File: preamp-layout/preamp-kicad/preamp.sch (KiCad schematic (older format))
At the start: 13 parts, among them J1 AudioJack3, P1 Conn_WallPlug, SW1 SW_SPST, SW10 Rotary_Encoder_Switch, SW11 Rotary_Encoder_Switch, SW2 SW_Push_Open, SW3 SW_Push_Open, SW4 SW_Push_Open, SW5 SW_Push_Open, SW6 SW_Push_Open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

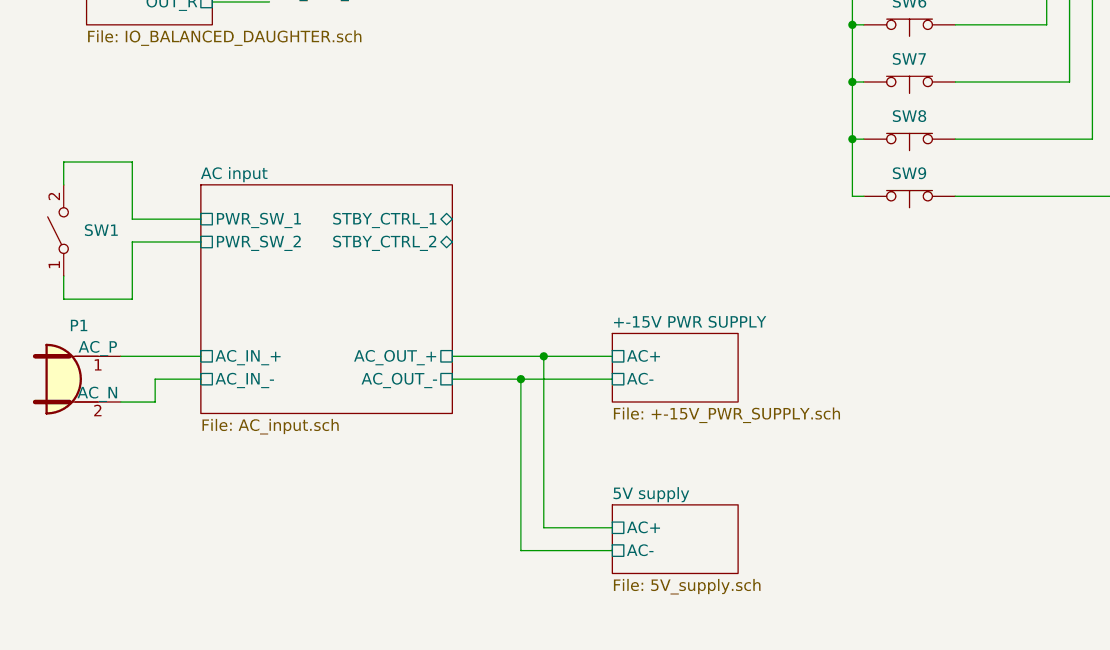
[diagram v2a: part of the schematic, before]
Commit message: Power Supply Update
Grounding made more clear, tied to chassis on AC board. Pins renamed. Aligned with AC wall power convention. General cleanup.
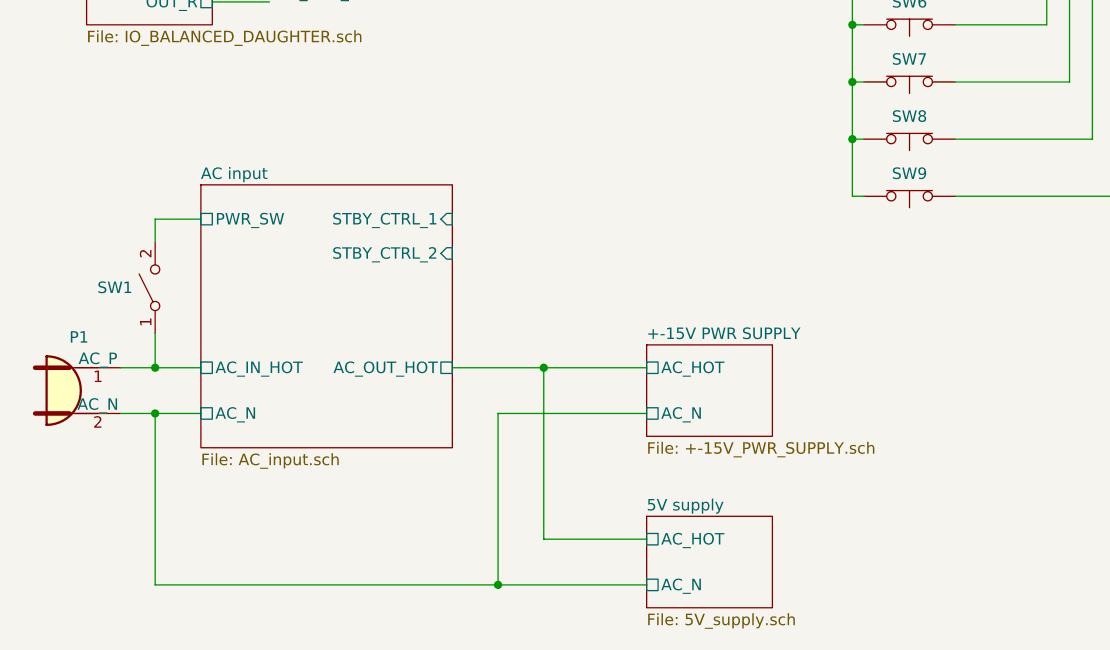
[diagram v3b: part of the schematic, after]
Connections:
- net AC input/PWR_SW_2 is gone; now on net AC input/AC_IN_HOT: SW1.1 (A)
- net AC input/AC_IN_+ renamed AC input/AC_IN_HOT
- net AC input/AC_IN_- renamed +-15V PWR SUPPLY/AC_N
- net AC input/PWR_SW_1 renamed AC input/PWR_SW
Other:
- moved on the sheet: P1, SW1
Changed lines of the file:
@@
 $EndDescr
 $Sheet
-S 1650 5650 1100 1000
+S 1650 5650 1100 1150
 U 5E26F6FE
 F0 "AC input" 50
 F1 "AC_input.sch" 50
-F2 "PWR_SW_1" U L 1650 5800 50
-F3 "PWR_SW_2" U L 1650 5900 50
-F4 "AC_OUT_+" U R 2750 6400 50
-F5 "AC_IN_-" U L 1650 6500 50
-F6 "AC_IN_+" U L 1650 6400 50
-F7 "AC_OUT_-" U R 2750 6500 50
-F8 "STBY_CTRL_2" B R 2750 5900 50
-F9 "STBY_CTRL_1" B R 2750 5800 50
-$EndSheet
-$Sheet
-S 3450 6300 550  300
+F2 "AC_OUT_HOT" U R 2750 6450 50
+F3 "AC_IN_HOT" U L 1650 6450 50
+F4 "AC_N" U L 1650 6650 50
+F5 "PWR_SW" U L 1650 5800 50
+F6 "STBY_CTRL_2" I R 2750 5950 50
+F7 "STBY_CTRL_1" I R 2750 5800 50
+$EndSheet
+$Sheet
+S 3600 6350 550  400
 U 5E27B612
 F0 "+-15V PWR SUPPLY" 50
 F1 "+-15V_PWR_SUPPLY.sch" 50
-F2 "AC+" U L 3450 6400 50
-F3 "AC-" U L 3450 6500 50
-$EndSheet
-$Sheet
-S 3450 7050 550  300
+F2 "AC_HOT" U L 3600 6450 50
+F3 "AC_N" U L 3600 6650 50
+$EndSheet
+$Sheet
+S 3600 7100 550  400
 U 5E5EF2D4
 F0 "5V supply" 50
 F1 "5V_supply.sch" 50
-F2 "AC+" U L 3450 7150 50
-F3 "AC-" U L 3450 7250 50
+F2 "AC_HOT" U L 3600 7200 50
+F3 "AC_N" U L 3600 7400 50
 $EndSheet
 $Sheet
@@
 	8000 3500 8100 3600
 Wire Wire Line
-	2750 6400 3150 6400
-Wire Wire Line
-	2750 6500 3050 6500
-Wire Wire Line
-	3150 6400 3150 7150
-Wire Wire Line
-	3150 6400 3450 6400
-Wire Wire Line
-	3050 6500 3050 7250
-Wire Wire Line
-	3050 6500 3450 6500
+	2750 6450 3150 6450
+Wire Wire Line
+	3150 6450 3150 7200
 Wire Wire Line
 	1600 2850 2150 2850
@@
 Wire Wire Line
 	10750 2400 10750 2900
-$Comp
-L Switch:SW_SPST SW?
-U 1 1 5E2E8D21
-P 1050 5850
-AR Path="/5E26F6FE/5E2E8D21" Ref="SW?"  Part="1"
-AR Path="/5E2E8D21" Ref="SW1"  Part="1"
-F 0 "SW1" V 1050 5762 50  0000 R CNN
-F 1 "SW_SPST" H 1050 5994 50  0001 C CNN
-F 2 "" H 1050 5850 50  0001 C CNN
-F 3 "~" H 1050 5850 50  0001 C CNN
-	1    1050 5850
-	0    -1   -1   0
-$EndComp
-Wire Wire Line
-	1050 5650 1050 5550
-Wire Wire Line
-	1050 5550 1350 5550
-Wire Wire Line
-	1350 5550 1350 5800
-Wire Wire Line
-	1350 5800 1650 5800
-Wire Wire Line
-	1050 6050 1050 6150
-Wire Wire Line
-	1050 6150 1350 6150
-Wire Wire Line
-	1350 6150 1350 5900
-Wire Wire Line
-	1350 5900 1650 5900
-$Comp
-L Connector:Conn_WallPlug P?
-U 1 1 5E300B43
-P 1100 6500
-AR Path="/5E26F6FE/5E300B43" Ref="P?"  Part="1"
-AR Path="/5E300B43" Ref="P1"  Part="1"
-F 0 "P1" H 1117 6733 50  0000 C CNN
-F 1 "Conn_WallPlug" H 1117 6734 50  0001 C CNN
-F 2 "" H 1500 6500 50  0001 C CNN
-F 3 "~" H 1500 6500 50  0001 C CNN
-	1    1100 6500
-	1    0    0    -1
-$EndComp
-Wire Wire Line
-	1300 6400 1650 6400
-Wire Wire Line
-	1300 6600 1450 6600
-Wire Wire Line
-	1450 6600 1450 6500
-Wire Wire Line
-	1450 6500 1650 6500
 $Sheet
 S 8250 4500 550  300
@@
 F5 "IN_R" U R 1700 4600 50
 $EndSheet
-Connection ~ 3050 6500
-Connection ~ 3150 6400
-Wire Wire Line
-	3450 7150 3150 7150
-Wire Wire Line
-	3450 7250 3050 7250
+Connection ~ 3150 6450
 Wire Wire Line
 	7800 3050 7800 4650
@@
 Wire Wire Line
 	7650 2900 8200 2900
+Wire Wire Line
+	1300 6650 1450 6650
+$Comp
+L Connector:Conn_WallPlug P?
+U 1 1 5E300B43
+P 1100 6550
+AR Path="/5E26F6FE/5E300B43" Ref="P?"  Part="1"
+AR Path="/5E300B43" Ref="P1"  Part="1"
+F 0 "P1" H 1117 6783 50  0000 C CNN
+F 1 "Conn_WallPlug" H 1117 6784 50  0001 C CNN
+F 2 "" H 1500 6550 50  0001 C CNN
+F 3 "~" H 1500 6550 50  0001 C CNN
+	1    1100 6550
+	1    0    0    -1
+$EndComp
+$Comp
+L Switch:SW_SPST SW?
+U 1 1 5E2E8D21
+P 1450 6100
+AR Path="/5E26F6FE/5E2E8D21" Ref="SW?"  Part="1"
+AR Path="/5E2E8D21" Ref="SW1"  Part="1"
+F 0 "SW1" V 1450 6198 50  0000 L CNN
+F 1 "SW_SPST" H 1450 6244 50  0001 C CNN
+F 2 "" H 1450 6100 50  0001 C CNN
+F 3 "~" H 1450 6100 50  0001 C CNN
+	1    1450 6100
+	0    -1   -1   0
+$EndComp
+Wire Wire Line
+	1300 6450 1450 6450
+Wire Wire Line
+	1450 5900 1450 5800
+Wire Wire Line
+	1450 5800 1650 5800
+Wire Wire Line
+	1450 6300 1450 6450
+Connection ~ 1450 6450
+Wire Wire Line
+	1450 6450 1650 6450
+Wire Wire Line
+	1450 7400 2950 7400
+Connection ~ 1450 6650
+Wire Wire Line
+	1450 6650 1650 6650
+Connection ~ 2950 7400
+Wire Wire Line
+	2950 6650 2950 7400
+Wire Wire Line
+	1450 6650 1450 7400
+Wire Wire Line
+	3150 6450 3600 6450
+Wire Wire Line
+	2950 6650 3600 6650
+Wire Wire Line
+	3150 7200 3600 7200
+Wire Wire Line
+	2950 7400 3600 7400
 Wire Bus Line
 	5200 1700 5200 3300

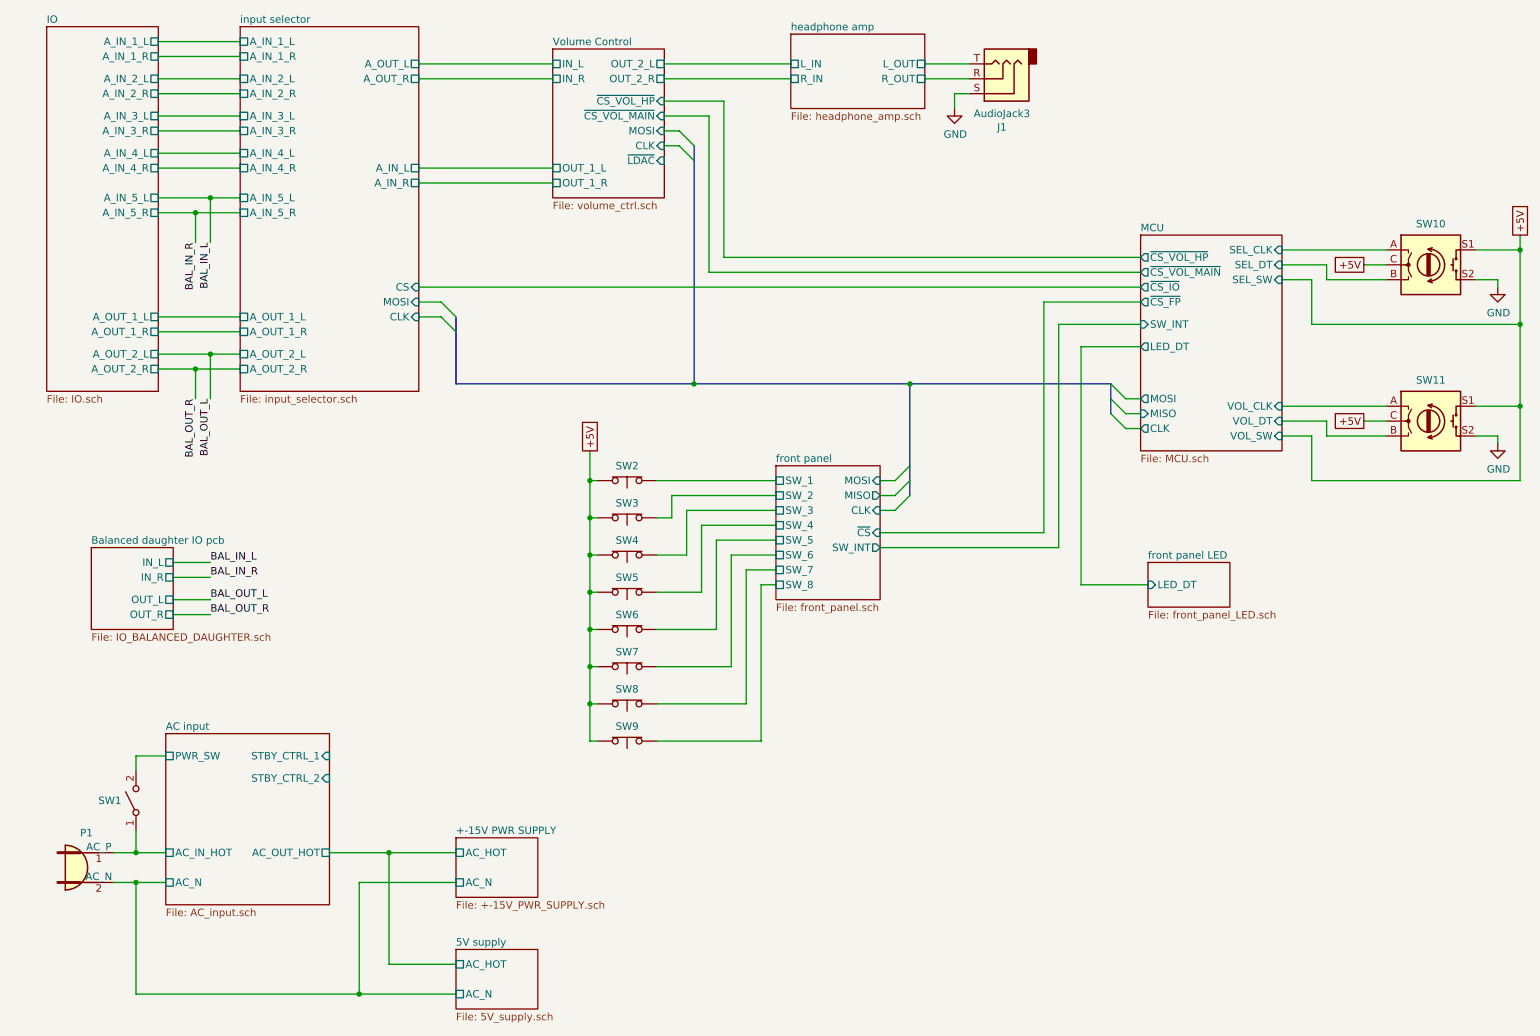
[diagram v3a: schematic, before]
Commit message: Schematic layout updates
schematic optimization. Also implemented encoders with surrounding circuitry (self-contained on encoder board)
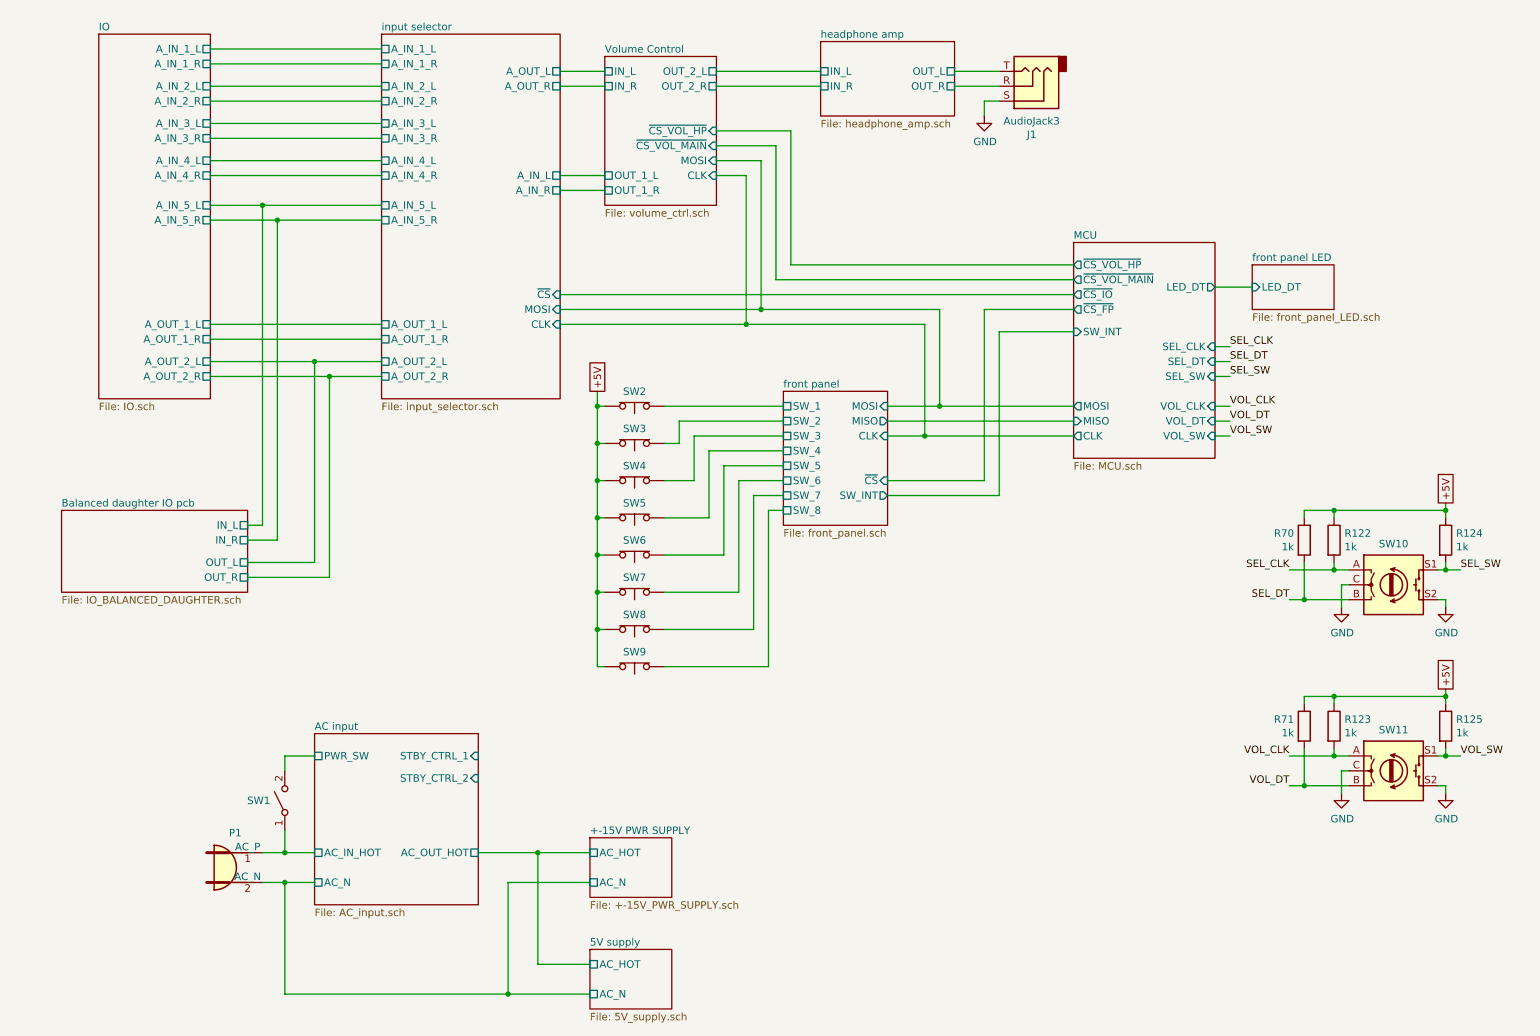
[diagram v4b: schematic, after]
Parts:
- added R122, R123, R124, R125, R70, R71: 1k, Resistor_SMD:R_1206_3216Metric_Pad1.42x1.75mm_HandSolder, symbol Device:R
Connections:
- net +5V: now also R122.1, R123.1, R124.1, R125.1, R70.1, R71.1; no longer SW10.C, SW10.S1, SW11.C, SW11.S1
- net GND: now also SW10.C, SW11.C
- net MCU/SEL_CLK renamed SEL_CLK
- net SEL_CLK: now also R122.2
- net MCU/SEL_DT renamed SEL_DT
- net SEL_DT: now also R70.2
- net MCU/VOL_CLK renamed VOL_CLK
- net VOL_CLK: now also R123.2
- net MCU/VOL_DT renamed VOL_DT
- net VOL_DT: now also R71.2
- net headphone amp/L_OUT renamed headphone amp/OUT_L
- net headphone amp/R_OUT renamed headphone amp/OUT_R
- new net SEL_SW: R124.2, SW10.S1
- new net VOL_SW: R125.2, SW11.S1
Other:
- moved on the sheet: J1, P1, SW1, SW2, SW3, SW4, SW5, SW6, SW7, SW8, SW9

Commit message: I2C init commit
Changed design from using SPI interface to I2C interface, with exception of front LED array (SPI).
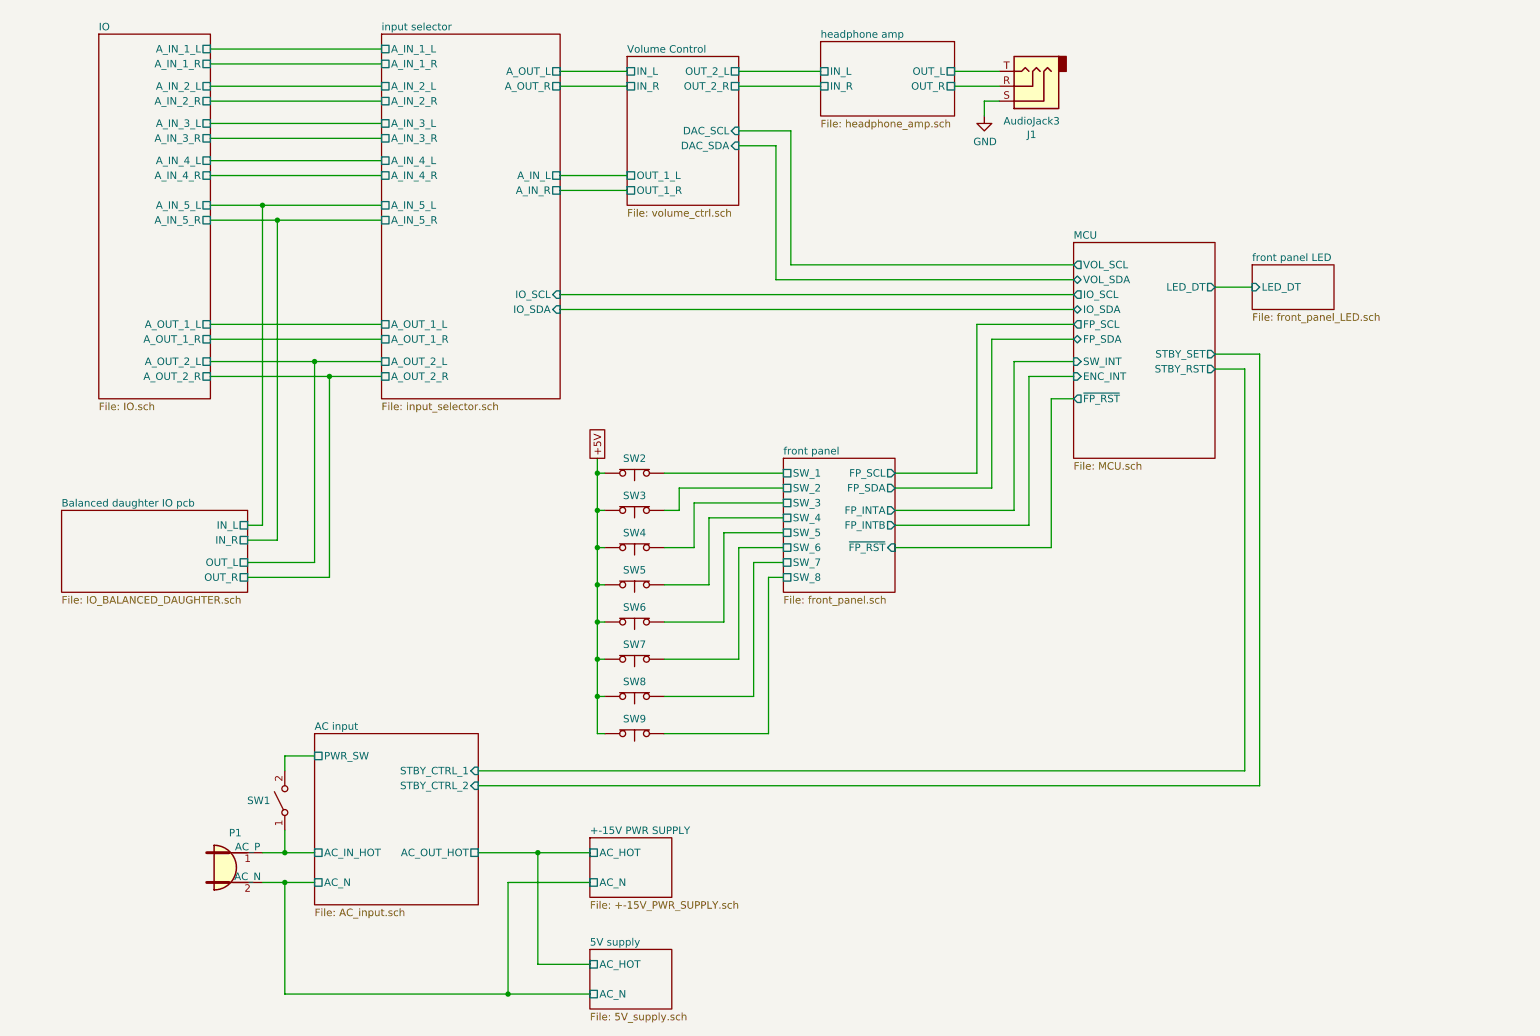
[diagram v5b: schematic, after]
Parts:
- removed R122, R123, R124, R125, R70, R71: 1k, Resistor_SMD:R_1206_3216Metric_Pad1.42x1.75mm_HandSolder, symbol Device:R
- removed SW10, SW11: Rotary_Encoder_Switch, symbol Device:Rotary_Encoder_Switch
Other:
- moved on the sheet: SW2, SW3, SW4, SW5, SW6, SW7, SW8, SW9

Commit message: BOM Update
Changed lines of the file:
@@
 $EndSheet
 $Sheet
-S 7750 2350 950  1450
+S 7750 2350 950  1200
 U 619FA14B
 F0 "MCU" 50

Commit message: Minor Updates
Moved headphone jack to amp pcb. I2C pin updates. Added caps to LED light strip. Added 0.1uF caps to all ICs.
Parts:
- removed J1: AudioJack3, symbol Connector:AudioJack3
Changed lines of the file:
@@
-$EndSheet
-$Sheet
-S 5800 3800 750  900
-U 5E5ECAAE
-F0 "front panel" 50
-F1 "front_panel.sch" 50
-F2 "SW_1" U L 5800 3900 50
-F3 "SW_2" U L 5800 4000 50
-F4 "SW_3" U L 5800 4100 50
-F5 "SW_4" U L 5800 4200 50
-F6 "SW_5" U L 5800 4300 50
-F7 "SW_6" U L 5800 4400 50
-F8 "SW_7" U L 5800 4500 50
-F9 "SW_8" U L 5800 4600 50
-F10 "FP_INTB" O R 6550 4250 50
-F11 "FP_SCL" O R 6550 3900 50
-F12 "FP_INTA" O R 6550 4150 50
-F13 "FP_SDA" O R 6550 4000 50
-F14 "~FP_RST" I R 6550 4400 50
 $EndSheet
 $Sheet
@@
 F2 "LED_DT" O R 8700 2650 50
 F3 "SW_INT" I L 7750 3150 50
-F4 "IO_SDA" B L 7750 2800 50
-F5 "IO_SCL" O L 7750 2700 50
-F6 "VOL_SDA" B L 7750 2600 50
-F7 "VOL_SCL" O L 7750 2500 50
-F8 "FP_SDA" B L 7750 3000 50
-F9 "FP_SCL" O L 7750 2900 50
-F10 "ENC_INT" I L 7750 3250 50
-F11 "~FP_RST" O L 7750 3400 50
-F12 "STBY_SET" O R 8700 3100 50
-F13 "STBY_RST" O R 8700 3200 50
+F4 "IO_SCL" O L 7750 2700 50
+F5 "VOL_SCL" O L 7750 2500 50
+F6 "FP_SCL" O L 7750 2900 50
+F7 "ENC_INT" I L 7750 3250 50
+F8 "~FP_RST" O L 7750 3400 50
+F9 "STBY_SET" O R 8700 3100 50
+F10 "STBY_RST" O R 8700 3200 50
+F11 "IO_SDA" O L 7750 2800 50
+F12 "VOL_SDA" O L 7750 2600 50
+F13 "FP_SDA" I L 7750 3000 50
 $EndSheet
 $Sheet
@@
 F9 "DAC_SDA" I R 5500 1700 50
 $EndSheet
-$Comp
-L Connector:AudioJack3 J?
-U 1 1 5F4B3F32
-P 7450 1300
-AR Path="/5E4A803E/5F4B3F32" Ref="J?"  Part="1"
-AR Path="/5F4B3F32" Ref="J1"  Part="1"
-F 0 "J1" H 7432 1625 50  0000 C CNN
-F 1 "AudioJack3" H 7432 1534 50  0000 C CNN
-F 2 "" H 7450 1300 50  0001 C CNN
-F 3 "~" H 7450 1300 50  0001 C CNN
-	1    7450 1300
-	-1   0    0    1
-$EndComp
-$Comp
-L power:GND #PWR?
-U 1 1 5F4B3F39
-P 7150 1500
-AR Path="/6009D432/5F4B3F39" Ref="#PWR?"  Part="1"
-AR Path="/5E4A803E/5F4B3F39" Ref="#PWR?"  Part="1"
-AR Path="/5F4B3F39" Ref="#PWR01"  Part="1"
-F 0 "#PWR01" H 7150 1250 50  0001 C CNN
-F 1 "GND" H 7155 1327 50  0000 C CNN
-F 2 "" H 7150 1500 50  0001 C CNN
-F 3 "" H 7150 1500 50  0001 C CNN
-	1    7150 1500
-	1    0    0    -1
-$EndComp
-Wire Wire Line
-	7150 1500 7150 1400
-Wire Wire Line
-	7150 1400 7250 1400
-Wire Wire Line
-	6950 1200 7250 1200
-Wire Wire Line
-	6950 1300 7250 1300
 $Sheet
 S 6050 1000 900  500
@@
 F0 "headphone amp" 50
 F1 "headphone_amp.sch" 50
-F2 "OUT_L" U R 6950 1200 50
-F3 "OUT_R" U R 6950 1300 50
 F4 "IN_L" U L 6050 1200 50
 F5 "IN_R" U L 6050 1300 50
@@
 Wire Wire Line
 	5500 1700 5750 1700
+$Sheet
+S 5800 3800 750  900
+U 5E5ECAAE
+F0 "front panel" 50
+F1 "front_panel.sch" 50
+F2 "SW_1" U L 5800 3900 50
+F3 "SW_2" U L 5800 4000 50
+F4 "SW_3" U L 5800 4100 50
+F5 "SW_4" U L 5800 4200 50
+F6 "SW_5" U L 5800 4300 50
+F7 "SW_6" U L 5800 4400 50
+F8 "SW_7" U L 5800 4500 50
+F9 "SW_8" U L 5800 4600 50
+F10 "FP_INTB" O R 6550 4250 50
+F11 "FP_INTA" O R 6550 4150 50
+F12 "~FP_RST" I R 6550 4400 50
+F13 "FP_SCL" I R 6550 3900 50
+F14 "FP_SDA" O R 6550 4000 50
+$EndSheet
 $EndSCHEMATC
